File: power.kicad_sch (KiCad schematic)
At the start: 6 parts, among them U3 INA260AIPW, U7 AZ1117IH-3.3TRG1

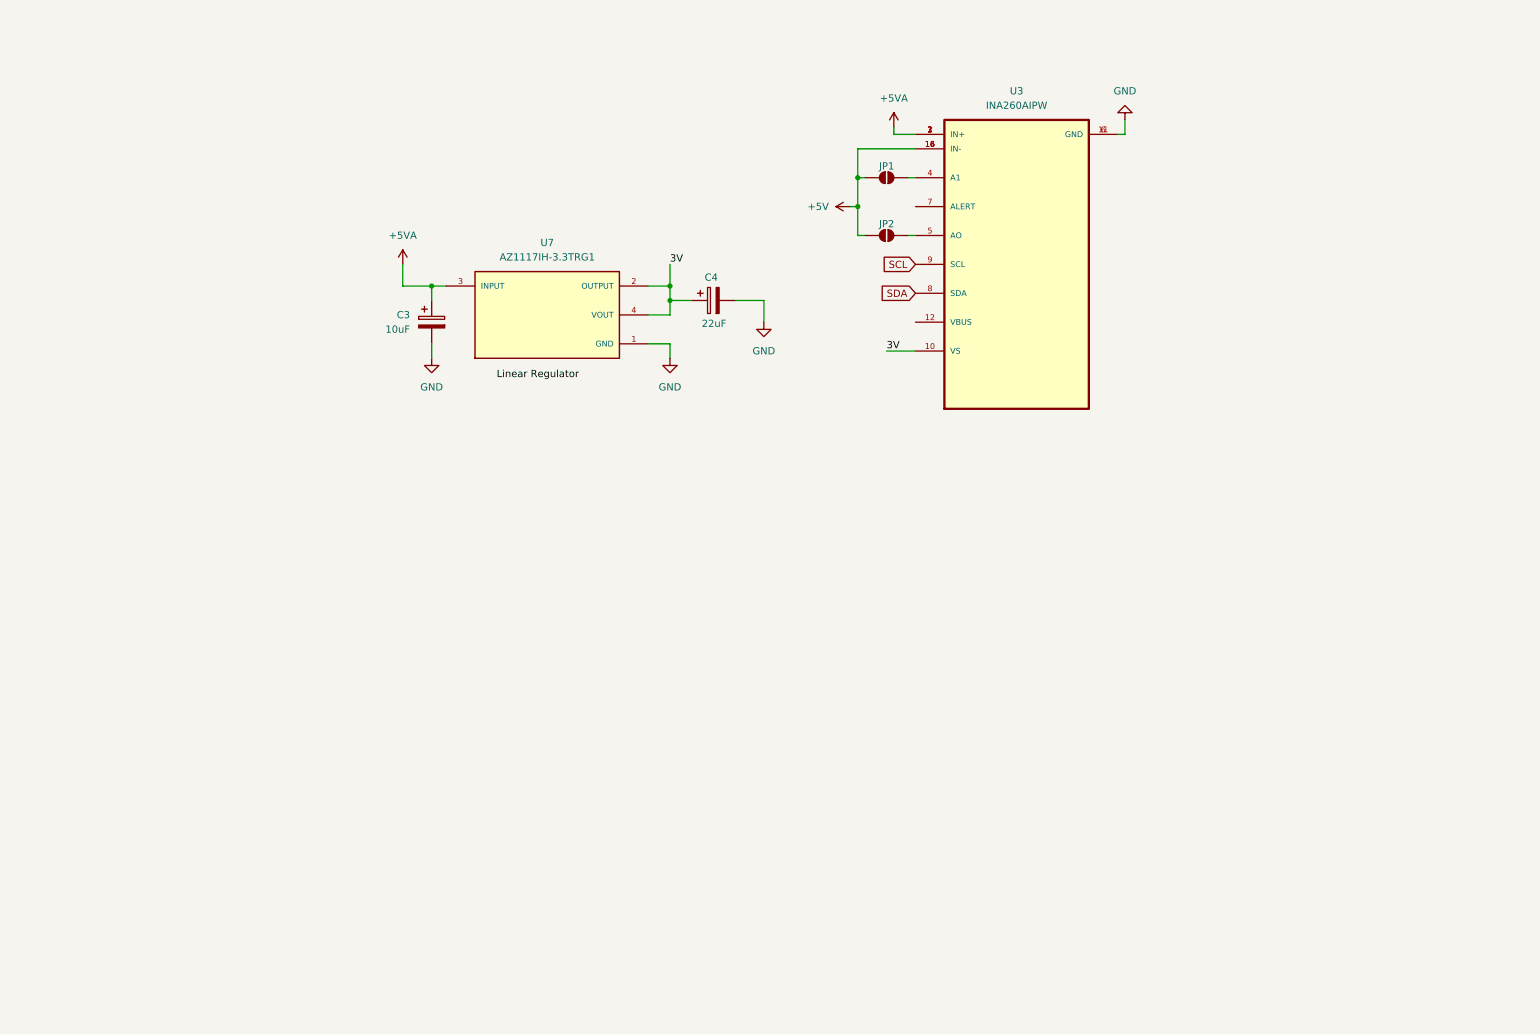
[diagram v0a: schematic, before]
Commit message: Added New Libraries and Schematic Updates
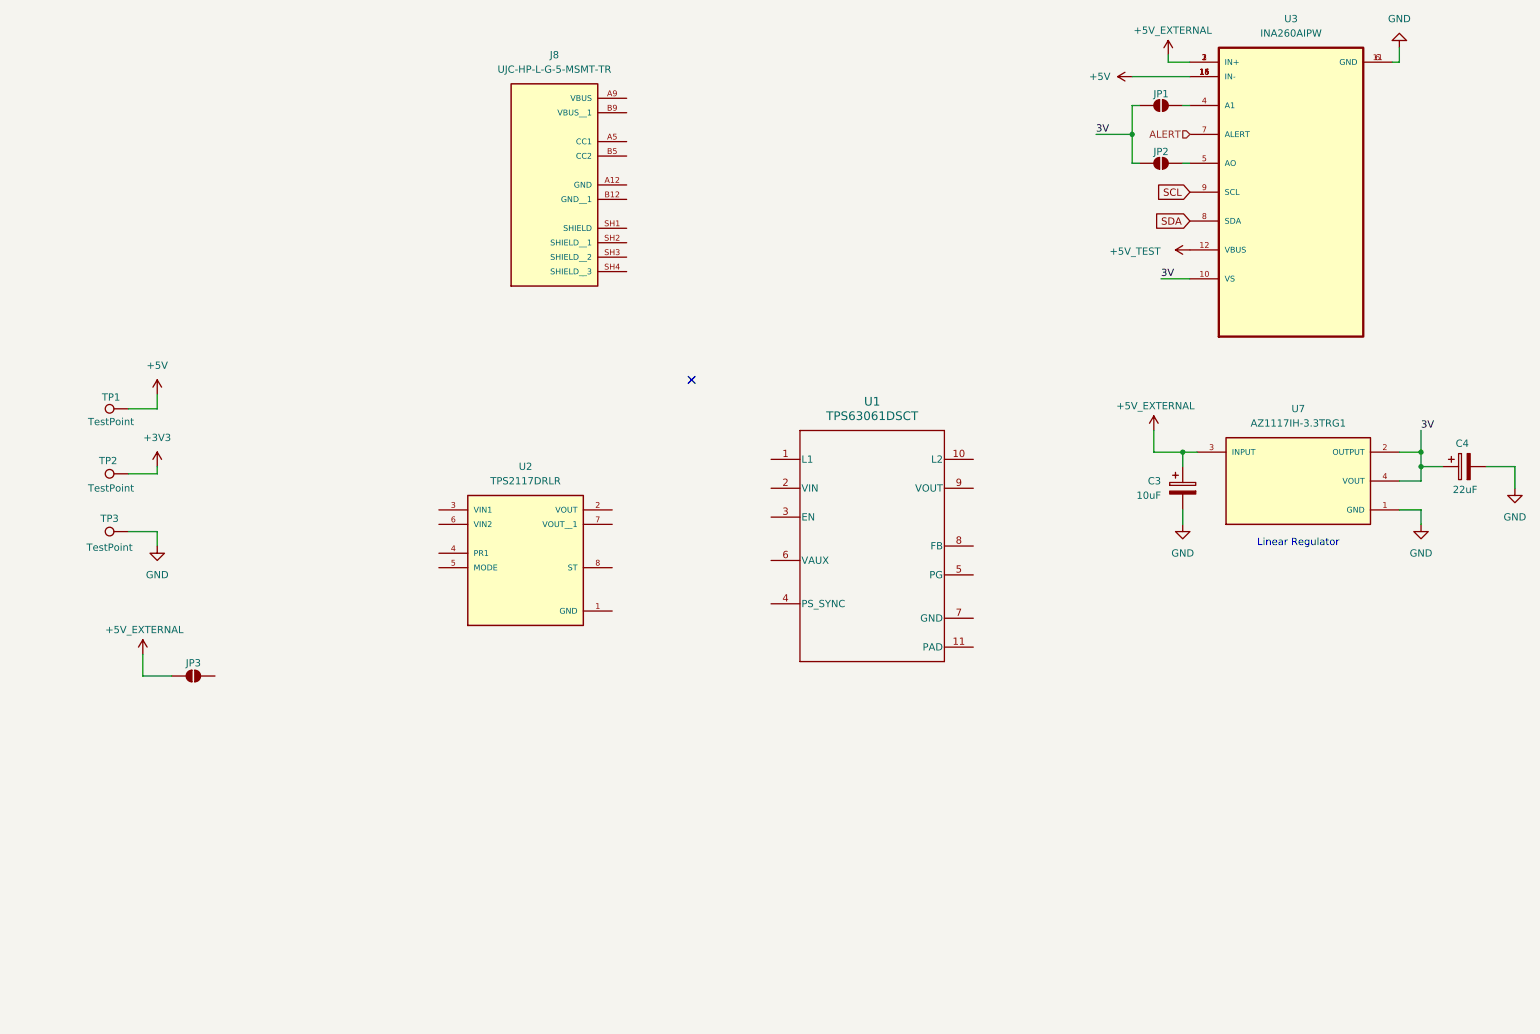
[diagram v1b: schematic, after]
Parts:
- added J8: UJC-HP-L-G-5-MSMT-TR, UJC-HP-L-G-5-MSMT-TR:CUI_UJC-HP-L-G-5-MSMT-TR, symbol UJC-HP-L-G-5-MSMT-TR:UJC-HP-L-G-5-MSMT-TR
- added JP3: SolderJumper_2_Open, symbol Jumper:SolderJumper_2_Open
- added TP1, TP2, TP3: TestPoint, symbol Connector:TestPoint
- added U1: TPS63061DSCT, DSC0010E, symbol TPS63061DSCT:TPS63061DSCT
- added U2: TPS2117DRLR, TPS2117DRLR:SOTFL50P160X60-8N, symbol TPS2117DRLR:TPS2117DRLR
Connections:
- net +5V: now also TP1.1; no longer JP1.1 (A), JP2.1 (A)
- net 3V: now also JP1.1 (A), JP2.1 (A)
- net GND: now also TP3.1
- net +5V_TEST: now reaches U3.12 (VBUS)
- net ALERT: now reaches U3.7 (ALERT)
- net +5VA renamed +5V_EXTERNAL
- net +5V_EXTERNAL: now also JP3.1 (A)
- new net +3V3: TP2.1
- no-connect marks 0 -> 1
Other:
- note added: "Linear Regulator"
- moved on the sheet: C3, C4, JP1, JP2, U3, U7

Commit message: Root Update and Adding ISO Pt1
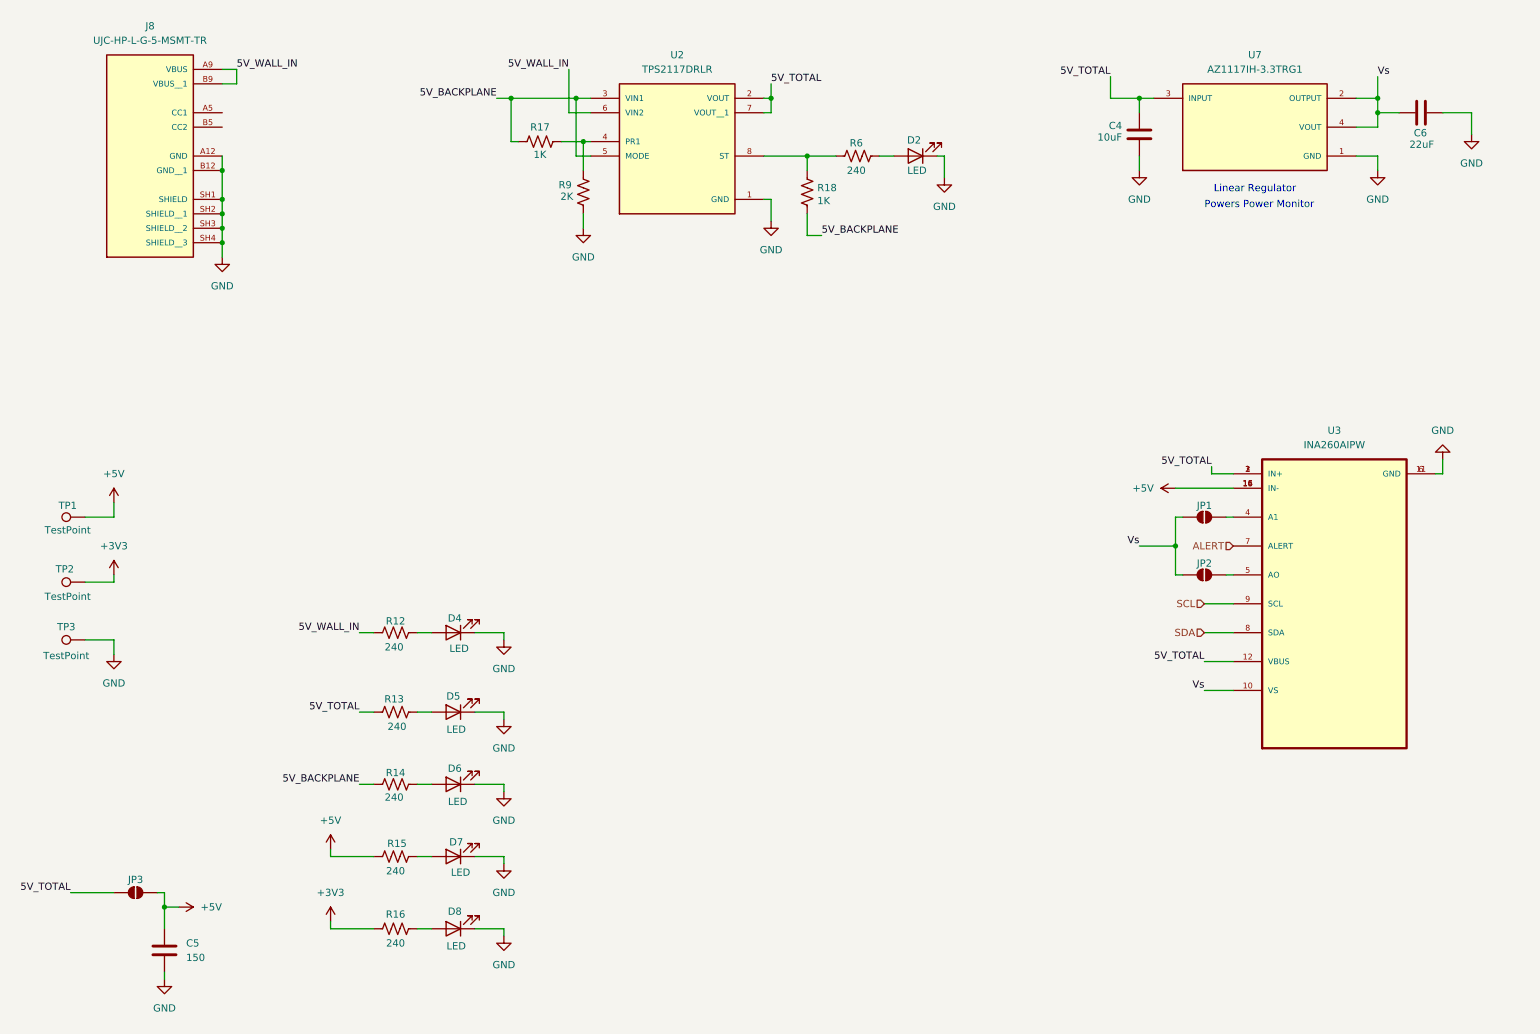
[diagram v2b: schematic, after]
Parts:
- removed C3: 10uF, symbol Device:C_Polarized
- removed C4: 22uF, symbol Device:C_Polarized
- removed U1: TPS63061DSCT, DSC0010E, symbol TPS63061DSCT:TPS63061DSCT
- added C4: 10uF, symbol Device:C
- added C5: 150, symbol Device:C
- added C6: 22uF, symbol Device:C
- added D2, D4, D5, D6, D7, D8: LED, symbol Device:LED
- added R12, R13, R14, R15, R16, R6: 240, symbol Device:R_US
- added R17, R18: 1K, symbol Device:R_US
- added R9: 2K, symbol Device:R_US
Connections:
- net +5V_EXTERNAL is gone; now on net 5V_TOTAL: JP3.1 (A), U3.1 (IN+), U3.2 (IN+), U3.3 (IN+), U7.3 (INPUT)
- net +5V_TEST is gone; now on net 5V_TOTAL: U3.12 (VBUS)
- net +3V3: now also R16.1
- net +5V: now also JP3.2 (B), C5.1, R15.1
- net GND: now also J8.A12 (GND), J8.B12 (GND__1), J8.SH1 (SHIELD), J8.SH2 (SHIELD__1), J8.SH3 (SHIELD__2), J8.SH4 (SHIELD__3), U2.1 (GND), C4.2, C5.2, C6.2, D2.1 (K), D4.1 (K), D5.1 (K), D6.1 (K), D7.1 (K), D8.1 (K), R9.1
- net 5V_TOTAL: now reaches U2.2 (VOUT)
- net 5V_TOTAL: now also U2.7 (VOUT__1), C4.1, R13.1
- net 5V_BACKPLANE: now reaches U2.3 (VIN1)
- net 5V_BACKPLANE: now also U2.5 (MODE), R14.1, R17.2, R18.2
- net at U2.4 (PR1): now also R17.1, R9.2
- net 5V_WALL_IN: now reaches U2.6 (VIN2)
- net 5V_WALL_IN: now also J8.A9 (VBUS), J8.B9 (VBUS__1), R12.1
- net at U2.8 (ST): now also R18.1, R6.1
- net 3V renamed Vs
- net Vs: now also C6.1
- new net: D2.2 (A), R6.2
- new net: D6.2 (A), R14.2
- new net: D7.2 (A), R15.2
- new net: D4.2 (A), R12.2
- new net: D5.2 (A), R13.2
- new net: D8.2 (A), R16.2
- no-connect marks 1 -> 0
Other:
- note added: "Powers Power Monitor"
- moved on the sheet: J8, JP1, JP2, JP3, TP1, TP2, TP3, U2, U3, U7

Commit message: Adding Libraries
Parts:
- added J20, J21: Conn_01x02_Pin, symbol Connector:Conn_01x02_Pin
- C5: value 150 -> 150uF
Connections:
- net +3V3: now also J20.1 (Pin_1), J21.1 (Pin_1)
- net GND: now also J20.2 (Pin_2), J21.2 (Pin_2)
- no-connect marks 0 -> 2
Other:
- note added: "3V3 Headers"
- moved on the sheet: D4, D5, D6, D7, D8, JP1, JP2, R12, R13, R14, R15, R16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

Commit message: Finalizing Schematic
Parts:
- removed R17: 1K, symbol Device:R_US
- removed R9: 2K, symbol Device:R_US
- added C17: 150uF, symbol Device:C
- added C19, C20: 0.1uF, symbol Device:C
- added JP4: SolderJumper_2_Open, symbol Jumper:SolderJumper_2_Open
- added R21: 1K, symbol Device:R_US
- added R22: 2K, symbol Device:R_US
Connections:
- net 5V_BACKPLANE: now also C19.2, JP4.1 (A), R21.1
- net 5V_TOTAL: now also C17.1, JP4.2 (B)
- net 5V_WALL_IN: now also C20.1
- net GND: now also C17.2, C19.1, C20.2, R22.2
- net at U2.4 (PR1): now also R21.2, R22.1
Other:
- note added: "Bypass Power Jumpers"
- note added: "Power MUX"
- note added: "Power Monitor"
- note added: "Power Test Pads"
- note added: "Test LEDS"
- note added: "USB-C Connector"
- note removed: "Powers Power Monitor"
- moved on the sheet: C5, D4, D5, D6, D7, D8, J20, J21, JP1, JP2, JP3, R12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

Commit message: Final Schematic Update
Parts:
- removed C4: 10uF, symbol Device:C
- removed C6: 22uF, symbol Device:C
- removed U7: AZ1117IH-3.3TRG1, AZ1117IH-3.3TRG1:SOT230P700X185-4N, symbol AZ1117IH-3.3TRG1:AZ1117IH-3.3TRG1
- added C18: 10uF, symbol Device:C
- added C21: 22uF, symbol Device:C
- added U4: AZ1117IH-3.3TRG1, SOT223_AZ1117I_6P5X3P5_DIO, symbol AZ1117IH_3_3TRG1:AZ1117IH-3.3TRG1
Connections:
- net 5V_TOTAL: now also C18.1, U4.3 (INPUT); no longer U2.7 (VOUT__1)
- net GND: now also C18.2, C21.2, U4.1 (ADJ/GND)
- net Vs: now also C21.1, U4.2 (OUTPUT)
- no-connect marks 2 -> 3
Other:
- note added: "Power Flags"
- moved on the sheet: J8, JP1, JP2, TP1, TP2, TP3, U3

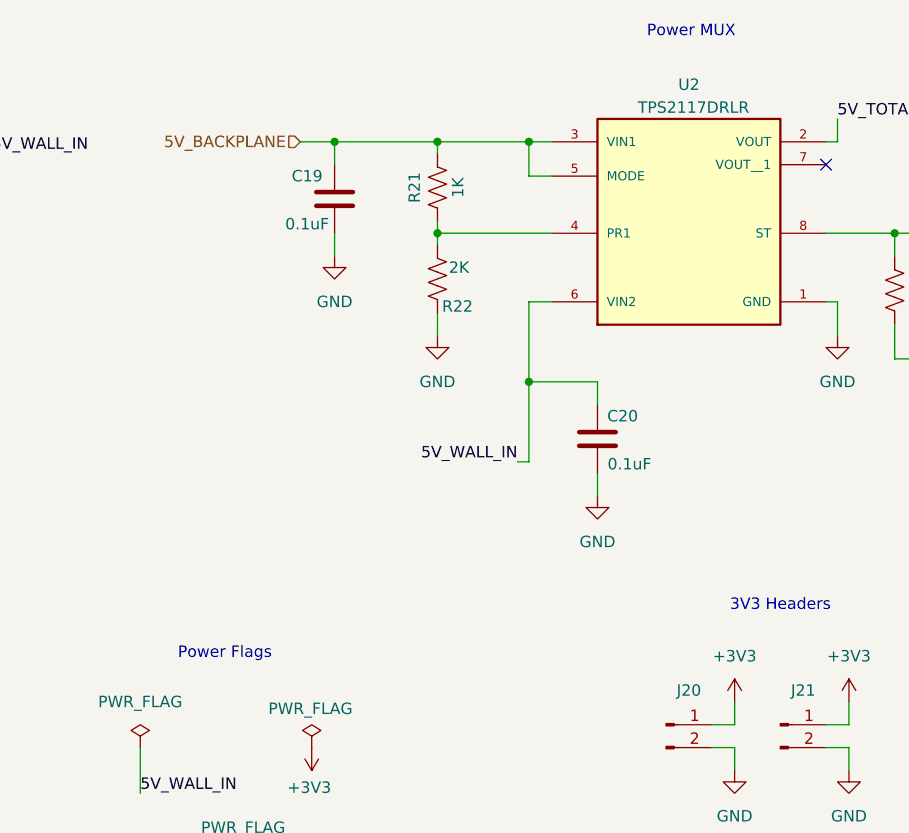
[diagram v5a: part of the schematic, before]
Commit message: Updated Hiearchal Root Sheet
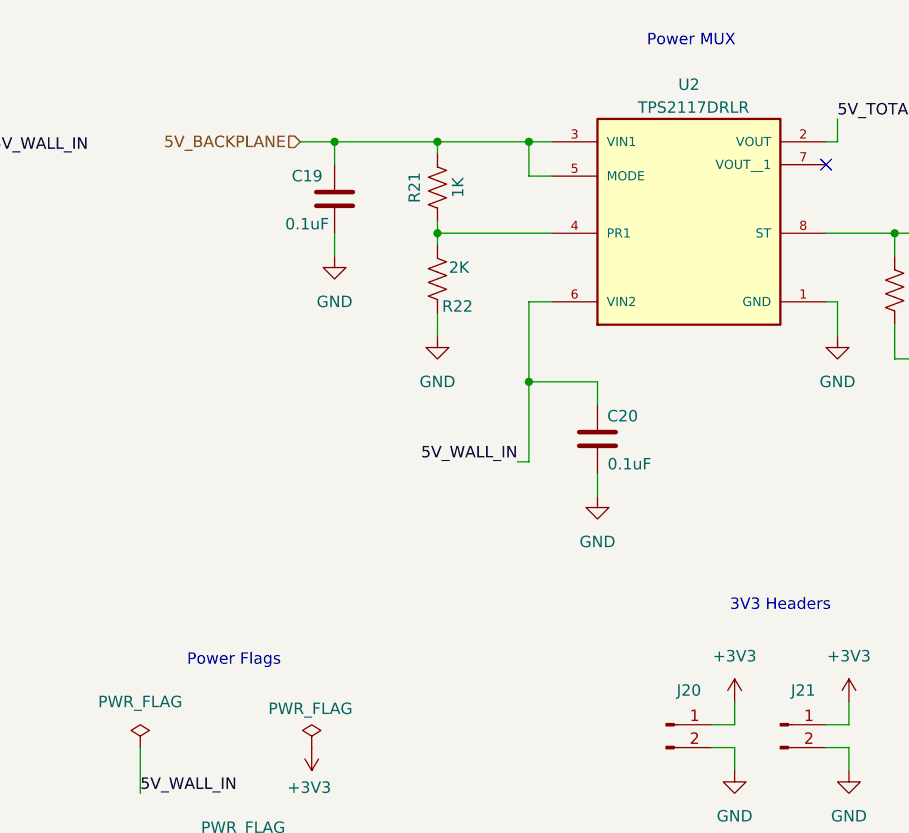
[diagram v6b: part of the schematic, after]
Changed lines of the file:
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@@
 	(text "Power MUX"
 		(exclude_from_sim no)
-		(at 131.064 20.828 0)
+		(at 131.064 21.844 0)
 		(effects
 			(font
@@
 	(text "Power Flags"
 		(exclude_from_sim no)
-		(at 79.248 89.916 0)
+		(at 80.264 90.678 0)
 		(effects
 			(font
